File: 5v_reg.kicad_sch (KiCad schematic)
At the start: 19 parts, among them U3 IR3899A

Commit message: Added indicator LEDs and fixed some footprints
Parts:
- C16, C17, C18, C19, C26, C27, C28, Cboot, Cin, Co, Cvcc, Cvin: footprint Capacitor_SMD:C_0805_2012Metric_Pad1.18x1.45mm_HandSolder -> Capacitor_SMD:C_0805_2012Metric
- Cff: footprint Capacitor_SMD:C_0603_1608Metric_Pad1.08x0.95mm_HandSolder -> Capacitor_SMD:C_0603_1608Metric
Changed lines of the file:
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@@
       (effects (font (size 1.27 1.27)) (justify left))
     )
-    (property "Footprint" "Capacitor_SMD:C_0805_2012Metric_Pad1.18x1.45mm_HandSolder" (at 159.7152 91.44 0)
+    (property "Footprint" "Capacitor_SMD:C_0805_2012Metric" (at 159.7152 91.44 0)
       (effects (font (size 1.27 1.27)) hide)
     )
@@
       (effects (font (size 1.27 1.27)) (justify left))
     )
-    (property "Footprint" "Capacitor_SMD:C_0805_2012Metric_Pad1.18x1.45mm_HandSolder" (at 88.5952 69.85 0)
+    (property "Footprint" "Capacitor_SMD:C_0805_2012Metric" (at 88.5952 69.85 0)
       (effects (font (size 1.27 1.27)) hide)
     )
@@
       (effects (font (size 1.27 1.27)) (justify left))
     )
-    (property "Footprint" "Capacitor_SMD:C_0805_2012Metric_Pad1.18x1.45mm_HandSolder" (at 106.3752 69.85 0)
+    (property "Footprint" "Capacitor_SMD:C_0805_2012Metric" (at 106.3752 69.85 0)
       (effects (font (size 1.27 1.27)) hide)
     )
@@
       (effects (font (size 1.27 1.27)) (justify left))
     )
-    (property "Footprint" "Capacitor_SMD:C_0603_1608Metric_Pad1.08x0.95mm_HandSolder" (at 197.8152 102.87 0)
+    (property "Footprint" "Capacitor_SMD:C_0603_1608Metric" (at 197.8152 102.87 0)
       (effects (font (size 1.27 1.27)) hide)
     )
@@
       (effects (font (size 1.27 1.27)) (justify left))
     )
-    (property "Footprint" "Capacitor_SMD:C_0805_2012Metric_Pad1.18x1.45mm_HandSolder" (at 160.9852 67.31 0)
+    (property "Footprint" "Capacitor_SMD:C_0805_2012Metric" (at 160.9852 67.31 0)
       (effects (font (size 1.27 1.27)) hide)
     )
@@
       (effects (font (size 1.27 1.27)) (justify left))
     )
-    (property "Footprint" "Capacitor_SMD:C_0805_2012Metric_Pad1.18x1.45mm_HandSolder" (at 219.4052 100.33 0)
+    (property "Footprint" "Capacitor_SMD:C_0805_2012Metric" (at 219.4052 100.33 0)
       (effects (font (size 1.27 1.27)) hide)
     )
@@
       (effects (font (size 1.27 1.27)) (justify left))
     )
-    (property "Footprint" "Capacitor_SMD:C_0805_2012Metric_Pad1.18x1.45mm_HandSolder" (at 96.2152 69.85 0)
+    (property "Footprint" "Capacitor_SMD:C_0805_2012Metric" (at 96.2152 69.85 0)
       (effects (font (size 1.27 1.27)) hide)
     )
@@
       (effects (font (size 1.27 1.27)) (justify left))
     )
-    (property "Footprint" "Capacitor_SMD:C_0805_2012Metric_Pad1.18x1.45mm_HandSolder" (at 119.0752 69.85 0)
+    (property "Footprint" "Capacitor_SMD:C_0805_2012Metric" (at 119.0752 69.85 0)
       (effects (font (size 1.27 1.27)) hide)
     )
@@
       (effects (font (size 1.27 1.27)) (justify left))
     )
-    (property "Footprint" "Capacitor_SMD:C_0805_2012Metric_Pad1.18x1.45mm_HandSolder" (at 234.6452 100.33 0)
+    (property "Footprint" "Capacitor_SMD:C_0805_2012Metric" (at 234.6452 100.33 0)
       (effects (font (size 1.27 1.27)) hide)
     )
@@
       (effects (font (size 1.27 1.27)) (justify left))
     )
-    (property "Footprint" "Capacitor_SMD:C_0805_2012Metric_Pad1.18x1.45mm_HandSolder" (at 246.0752 100.33 0)
+    (property "Footprint" "Capacitor_SMD:C_0805_2012Metric" (at 246.0752 100.33 0)
       (effects (font (size 1.27 1.27)) hide)
     )
@@
       (effects (font (size 1.27 1.27)) (justify left))
     )
-    (property "Footprint" "Capacitor_SMD:C_0805_2012Metric_Pad1.18x1.45mm_HandSolder" (at 178.7652 99.06 0)
+    (property "Footprint" "Capacitor_SMD:C_0805_2012Metric" (at 178.7652 99.06 0)
       (effects (font (size 1.27 1.27)) hide)
     )
@@
       (effects (font (size 1.27 1.27)) (justify left))
     )
-    (property "Footprint" "Capacitor_SMD:C_0805_2012Metric_Pad1.18x1.45mm_HandSolder" (at 110.1852 85.09 0)
+    (property "Footprint" "Capacitor_SMD:C_0805_2012Metric" (at 110.1852 85.09 0)
       (effects (font (size 1.27 1.27)) hide)
     )
@@
       (effects (font (size 1.27 1.27)) (justify left))
     )
-    (property "Footprint" "Capacitor_SMD:C_0805_2012Metric_Pad1.18x1.45mm_HandSolder" (at 80.9752 69.85 0)
-      (effects (font (size 1.27 1.27)) hide)
-    )
+    (property "Footprint" "Capacitor_SMD:C_0805_2012Metric" (at 80.9752 69.85 0)
+      (effects (font (size 1.27 1.27)) hide)
+    )

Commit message: fixed some more footprints for resistors. 0201 -> 0603
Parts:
- R1, RFB1, RFB2, Rpg: footprint Resistor_SMD:R_0201_0603Metric -> Resistor_SMD:R_0603_1608Metric
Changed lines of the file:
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@@
       (effects (font (size 1.27 1.27)))
     )
-    (property "Footprint" "Resistor_SMD:R_0201_0603Metric" (at 152.654 82.804 90)
+    (property "Footprint" "Resistor_SMD:R_0603_1608Metric" (at 152.654 82.804 90)
       (effects (font (size 1.27 1.27)) hide)
     )
@@
       (effects (font (size 1.27 1.27)) (justify left))
     )
-    (property "Footprint" "Resistor_SMD:R_0201_0603Metric" (at 205.486 99.314 90)
+    (property "Footprint" "Resistor_SMD:R_0603_1608Metric" (at 205.486 99.314 90)
       (effects (font (size 1.27 1.27)) hide)
     )
@@
       (effects (font (size 1.27 1.27)) (justify left))
     )
-    (property "Footprint" "Resistor_SMD:R_0201_0603Metric" (at 205.486 109.474 90)
+    (property "Footprint" "Resistor_SMD:R_0603_1608Metric" (at 205.486 109.474 90)
       (effects (font (size 1.27 1.27)) hide)
     )
@@
       (effects (font (size 1.27 1.27)) (justify left))
     )
-    (property "Footprint" "Resistor_SMD:R_0201_0603Metric" (at 103.886 81.534 90)
-      (effects (font (size 1.27 1.27)) hide)
-    )
+    (property "Footprint" "Resistor_SMD:R_0603_1608Metric" (at 103.886 81.534 90)
+      (effects (font (size 1.27 1.27)) hide)
+    )

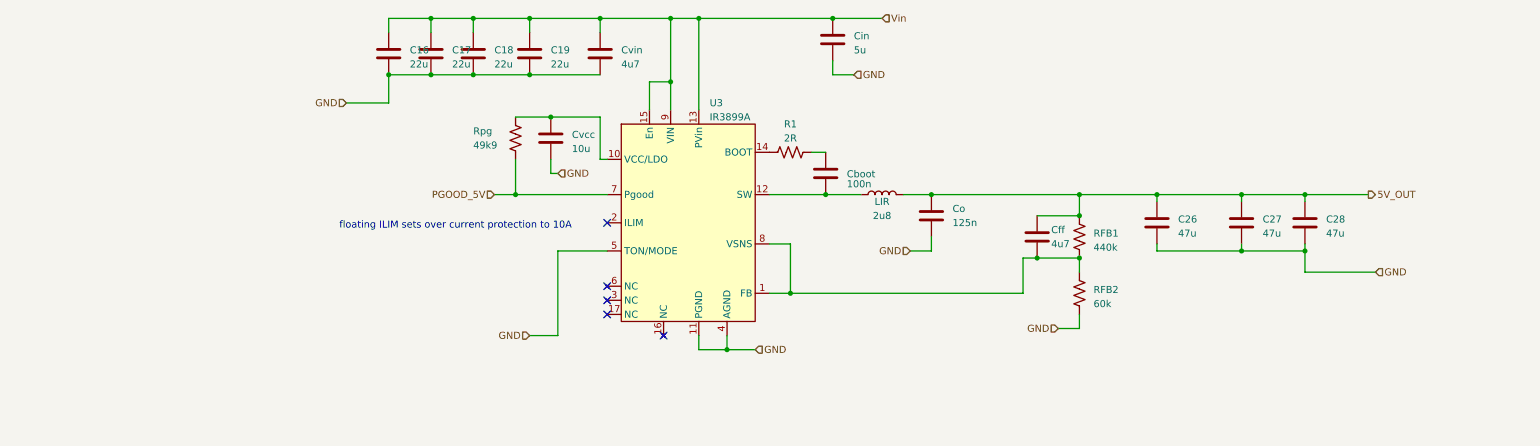
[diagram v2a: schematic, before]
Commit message: Changed 5V regulator and 12V regulator to the SiC461. Both support 10A and 5V and 12V respectively
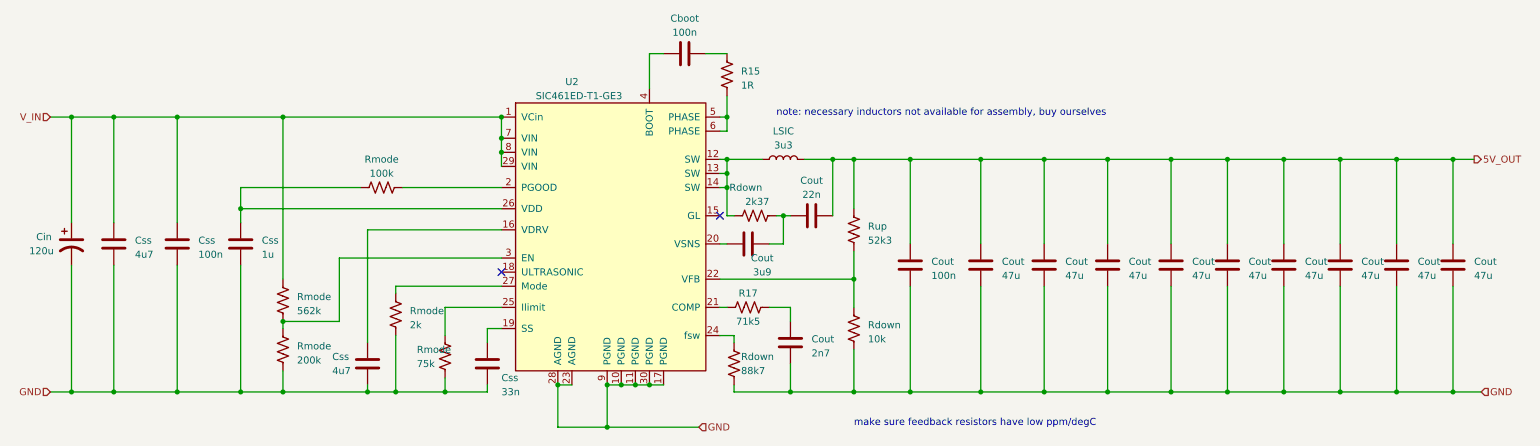
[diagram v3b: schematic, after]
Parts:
- removed C16, C17, C18, C19: 22u, Capacitor_SMD:C_0805_2012Metric, symbol Device:C
- removed C26, C27, C28: 47u, Capacitor_SMD:C_0805_2012Metric, symbol Device:C
- removed Cff: 4u7, Capacitor_SMD:C_0603_1608Metric, symbol Device:C
- removed Cin: 5u, Capacitor_SMD:C_0805_2012Metric, symbol Device:C
- removed Co: 125n, Capacitor_SMD:C_0805_2012Metric, symbol Device:C
- removed Cvcc: 10u, Capacitor_SMD:C_0805_2012Metric, symbol Device:C
- removed Cvin: 4u7, Capacitor_SMD:C_0805_2012Metric, symbol Device:C
- removed LIR: 2u8, crush-power-footprints:IND_1365-WE-HCI_WRE-L, symbol Device:L
- removed R1: 2R, Resistor_SMD:R_0603_1608Metric, symbol Device:R_US
- removed RFB1: 440k, Resistor_SMD:R_0603_1608Metric, symbol Device:R_US
- removed RFB2: 60k, Resistor_SMD:R_0603_1608Metric, symbol Device:R_US
- removed Rpg: 49k9, Resistor_SMD:R_0603_1608Metric, symbol Device:R_US
- removed U3: IR3899A, crush-power-footprints:IR3899AMTRPBFAUMA1, symbol crush-power-lib:IR3899A
- added Cin: 120u, Capacitor_Tantalum_SMD:CP_EIA-7343-15_Kemet-W, symbol Device:C_Polarized_US
- added Cout (x9): 47u, Capacitor_SMD:C_1210_3225Metric, symbol Device:C
- added Cout: 22n, Capacitor_SMD:C_0402_1005Metric, symbol Device:C
- added Cout: 3u9, Capacitor_SMD:C_0402_1005Metric, symbol Device:C
- added Cout, Css: 100n, Capacitor_SMD:C_0603_1608Metric, symbol Device:C
- added Cout: 2n7, Capacitor_SMD:C_0603_1608Metric, symbol Device:C
- added Css: 4u7, Capacitor_SMD:C_0603_1608Metric, symbol Device:C
- added Css: 33n, Capacitor_SMD:C_0603_1608Metric, symbol Device:C
- added Css: 4u7, Capacitor_SMD:C_0805_2012Metric, symbol Device:C
- added Css: 1u, Capacitor_SMD:C_0603_1608Metric, symbol Device:C
- added LSIC: 3u3, crush-power-footprints:IND_IHLP-6767GZ_VIS-M, symbol Device:L
- added R15: 1R, Resistor_SMD:R_0402_1005Metric, symbol Device:R_US
- added R17: 71k5, Resistor_SMD:R_0402_1005Metric, symbol Device:R_US
- added Rdown: 88k7, Resistor_SMD:R_0603_1608Metric, symbol Device:R_US
- added Rdown: 10k, Resistor_SMD:R_0603_1608Metric, symbol Device:R_US
- added Rdown: 2k37, Resistor_SMD:R_0402_1005Metric, symbol Device:R_US
- added Rmode: 75k, Resistor_SMD:R_0603_1608Metric, symbol Device:R_US
- added Rmode: 200k, Resistor_SMD:R_0603_1608Metric, symbol Device:R_US
- added Rmode: 562k, Resistor_SMD:R_0603_1608Metric, symbol Device:R_US
- added Rmode: 2k, Resistor_SMD:R_0603_1608Metric, symbol Device:R_US
- added Rmode: 100k, Resistor_SMD:R_0603_1608Metric, symbol Device:R_US
- added Rup: 52k3, Resistor_SMD:R_0603_1608Metric, symbol Device:R_US
- added U2: SIC461ED-T1-GE3, crush-power-footprints:CONV_SIC461ED-T1-GE3, symbol crush-power-lib:SIC461ED-T1-GE3
- Cboot: footprint Capacitor_SMD:C_0805_2012Metric -> Capacitor_SMD:C_0402_1005Metric
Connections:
- net 5V_OUT: now also Cout.1, Cout.1, Cout.1, Cout.1, Cout.1, Cout.1, Cout.1, Cout.1, Cout.1, Cout.1, Cout.2, LSIC.2, Rup.1
- net GND: now also Cin.2, Cout.2, Cout.2, Cout.2, Cout.2, Cout.2, Cout.2, Cout.2, Cout.2, Cout.2, Cout.2, Cout.2, Css.1, Css.1, Css.1, Css.1, Css.1, Rdown.2, Rdown.2, Rmode.1, Rmode.2, Rmode.2, U2.10 (PGND), U2.11 (PGND), U2.17 (PGND), U2.23 (AGND), U2.28 (AGND), U2.30 (PGND), U2.9 (PGND)
- net at Cboot.1: now also U2.4 (BOOT)
- net at Cboot.2: now also R15.2
- new net: R15.1, U2.5 (PHASE), U2.6 (PHASE)
- new net: Cout.1, Cout.2, Rdown.2
- new net: Css.2, U2.19 (SS)
- new net: Cout.1, U2.20 (VSNS)
- new net: R17.1, U2.21 (COMP)
- new net: Cout.1, R17.2
- new net: Css.2, U2.16 (VDRV)
- new net: Rdown.1, U2.24 (fsw)
- new net: Css.2, Rmode.1, U2.26 (VDD)
- new net: LSIC.1, Rdown.1, U2.12 (SW), U2.13 (SW), U2.14 (SW)
- new net: Rdown.1, Rup.2, U2.22 (VFB)
- new net: Rmode.2, U2.2 (PGOOD)
- new net: Rmode.1, U2.25 (Ilimit)
- new net: Rmode.1, U2.27 (Mode)
- new net: Rmode.1, Rmode.2, U2.3 (EN)
- new net V_IN: Cin.1, Css.2, Css.2, Rmode.2, U2.1 (VCin), U2.29 (VIN), U2.7 (VIN), U2.8 (VIN)
- no-connect marks 5 -> 2
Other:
- note added: "make sure feedback resistors have low ppm/degC"
- note added: "note: necessary inductors not available for assembly, buy ourselves"
- note removed: "floating ILIM sets over current protection to 10A"

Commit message: Added more to the layout of the 12V regulator as well as changed some capacitor footprints
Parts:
- Cin: footprint Capacitor_Tantalum_SMD:CP_EIA-7343-15_Kemet-W -> Capacitor_THT:CP_Radial_D8.0mm_P3.50mm
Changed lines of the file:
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@@
       (effects (font (size 1.27 1.27)) (justify left))
     )
-    (property "Footprint" "Capacitor_Tantalum_SMD:CP_EIA-7343-15_Kemet-W" (at 22.86 100.33 0)
+    (property "Footprint" "Capacitor_THT:CP_Radial_D8.0mm_P3.50mm" (at 22.86 100.33 0)
       (effects (font (size 1.27 1.27)) hide)
     )
@@
       (effects (font (size 1.27 1.27)) (justify bottom) hide)
     )
-    (property "Datasheet" "" (at 119.38 100.33 0)
-      (effects (font (size 1.27 1.27)) hide)
-    )
+    (property "Datasheet" "https://datasheet.lcsc.com/lcsc/2003271205_Vishay-Intertech-SIC461ED-T1-GE3_C499531.pdf" (at 119.38 100.33 0)
+      (effects (font (size 1.27 1.27)) hide)
+    )

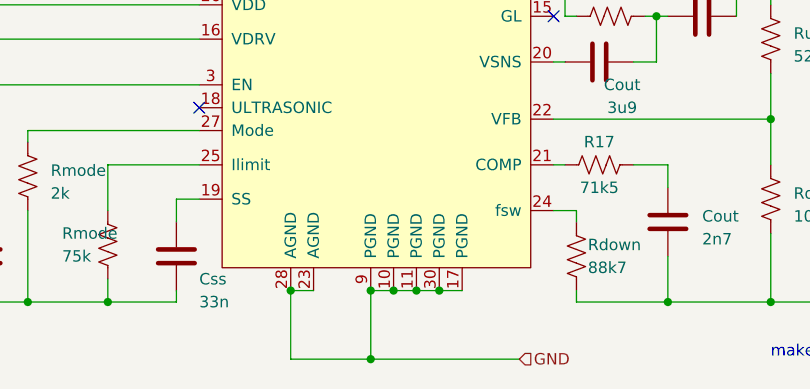
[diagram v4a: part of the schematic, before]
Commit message: Added thermal vias to the 12V regulator, fixed GND pad nets on 12V and 5V regulator
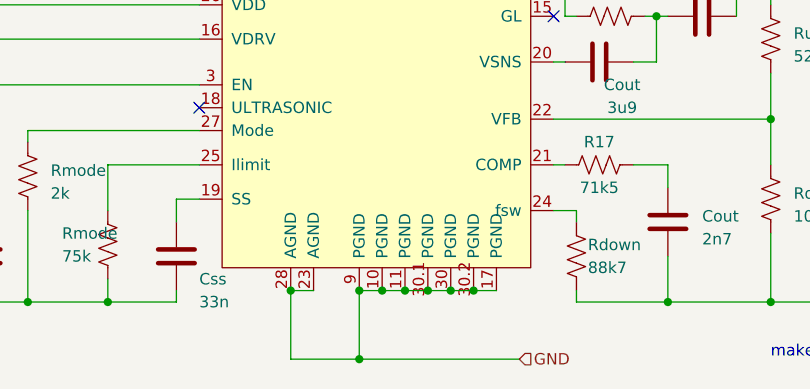
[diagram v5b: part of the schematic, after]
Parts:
- U2: footprint crush-power-footprints:CONV_SIC461ED-T1-GE3 -> CONV_SIC461ED-T1-GE3
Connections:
- net GND: now also U2.30.1 (PGND), U2.30.2 (PGND)
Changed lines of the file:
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@@
   (junction (at 53.34 93.98) (diameter 0) (color 0 0 0 0)
   )
-  (junction (at 119.38 125.73) (diameter 0) (color 0 0 0 0)
-  )
   (junction (at 251.46 127) (diameter 0) (color 0 0 0 0)
   )
@@
   (junction (at 30.48 127) (diameter 0) (color 0 0 0 0)
   )
+  (junction (at 125.73 125.73) (diameter 0) (color 0 0 0 0)
+  )
+  (junction (at 120.65 125.73) (diameter 0) (color 0 0 0 0)
+  )
   (junction (at 261.62 85.09) (diameter 0) (color 0 0 0 0)
   )
+  (junction (at 118.11 125.73) (diameter 0) (color 0 0 0 0)
+  )
   (junction (at 271.78 85.09) (diameter 0) (color 0 0 0 0)
   )
+  (junction (at 130.81 125.73) (diameter 0) (color 0 0 0 0)
+  )
   (junction (at 251.46 85.09) (diameter 0) (color 0 0 0 0)
   )
@@
   (junction (at 261.62 127) (diameter 0) (color 0 0 0 0)
   )
+  (junction (at 128.27 125.73) (diameter 0) (color 0 0 0 0)
+  )
   (junction (at 90.17 127) (diameter 0) (color 0 0 0 0)
   )
@@
   (junction (at 163.83 106.68) (diameter 0) (color 0 0 0 0)
   )
+  (junction (at 118.11 133.35) (diameter 0) (color 0 0 0 0)
+  )
   (junction (at 160.02 85.09) (diameter 0) (color 0 0 0 0)
   )
@@
   (junction (at 110.49 125.73) (diameter 0) (color 0 0 0 0)
   )
-  (junction (at 124.46 125.73) (diameter 0) (color 0 0 0 0)
-  )
   (junction (at 41.91 127) (diameter 0) (color 0 0 0 0)
   )
@@
   (junction (at 60.96 77.47) (diameter 0) (color 0 0 0 0)
   )
+  (junction (at 123.19 125.73) (diameter 0) (color 0 0 0 0)
+  )
   (junction (at 186.69 127) (diameter 0) (color 0 0 0 0)
   )
@@
   (junction (at 152.4 127) (diameter 0) (color 0 0 0 0)
   )
-  (junction (at 119.38 133.35) (diameter 0) (color 0 0 0 0)
-  )
   (junction (at 231.14 85.09) (diameter 0) (color 0 0 0 0)
   )
@@
   (junction (at 81.28 127) (diameter 0) (color 0 0 0 0)
   )
-  (junction (at 121.92 125.73) (diameter 0) (color 0 0 0 0)
-  )
   (junction (at 209.55 85.09) (diameter 0) (color 0 0 0 0)
   )
   (junction (at 198.12 85.09) (diameter 0) (color 0 0 0 0)
-  )
-  (junction (at 127 125.73) (diameter 0) (color 0 0 0 0)
   )
   (no_connect (at 139.7 95.25))
@@
     (stroke (width 0) (type default))
   )
-  (wire (pts (xy 119.38 133.35) (xy 135.89 133.35))
-    (stroke (width 0) (type default))
-  )
   (wire (pts (xy 140.97 80.01) (xy 139.7 80.01))
     (stroke (width 0) (type default))
@@
     (stroke (width 0) (type default))
   )
-  (wire (pts (xy 119.38 125.73) (xy 121.92 125.73))
-    (stroke (width 0) (type default))
-  )
   (wire (pts (xy 261.62 107.95) (xy 261.62 127))
     (stroke (width 0) (type default))
@@
     (stroke (width 0) (type default))
   )
-  (wire (pts (xy 119.38 125.73) (xy 119.38 133.35))
+  (wire (pts (xy 118.11 125.73) (xy 118.11 133.35))
+    (stroke (width 0) (type default))
+  )
+  (wire (pts (xy 128.27 125.73) (xy 130.81 125.73))
     (stroke (width 0) (type default))
   )
@@
     (stroke (width 0) (type default))
   )
+  (wire (pts (xy 118.11 133.35) (xy 135.89 133.35))
+    (stroke (width 0) (type default))
+  )
   (wire (pts (xy 271.78 127) (xy 276.86 127))
     (stroke (width 0) (type default))
@@
     (stroke (width 0) (type default))
   )
-  (wire (pts (xy 121.92 125.73) (xy 124.46 125.73))
-    (stroke (width 0) (type default))
-  )
   (wire (pts (xy 160.02 85.09) (xy 160.02 95.25))
     (stroke (width 0) (type default))
@@
     (stroke (width 0) (type default))
   )
-  (wire (pts (xy 124.46 125.73) (xy 127 125.73))
-    (stroke (width 0) (type default))
-  )
   (wire (pts (xy 261.62 85.09) (xy 261.62 100.33))
     (stroke (width 0) (type default))
@@
     (stroke (width 0) (type default))
   )
+  (wire (pts (xy 130.81 125.73) (xy 133.35 125.73))
+    (stroke (width 0) (type default))
+  )
   (wire (pts (xy 140.97 77.47) (xy 140.97 80.01))
     (stroke (width 0) (type default))
@@
     (stroke (width 0) (type default))
   )
-  (wire (pts (xy 127 125.73) (xy 129.54 125.73))
+  (wire (pts (xy 118.11 125.73) (xy 120.65 125.73))
     (stroke (width 0) (type default))
   )
@@
     (stroke (width 0) (type default))
   )
-  (wire (pts (xy 110.49 133.35) (xy 119.38 133.35))
+  (wire (pts (xy 110.49 133.35) (xy 118.11 133.35))
     (stroke (width 0) (type default))
   )
@@
     (stroke (width 0) (type default))
   )
+  (wire (pts (xy 125.73 125.73) (xy 128.27 125.73))
+    (stroke (width 0) (type default))
+  )
   (wire (pts (xy 173.99 127) (xy 186.69 127))
     (stroke (width 0) (type default))
@@
     (stroke (width 0) (type default))
   )
+  (wire (pts (xy 120.65 125.73) (xy 123.19 125.73))
+    (stroke (width 0) (type default))
+  )
   (wire (pts (xy 22.86 104.14) (xy 22.86 127))
     (stroke (width 0) (type default))
@@
   )
   (wire (pts (xy 129.54 66.04) (xy 127 66.04))
+    (stroke (width 0) (type default))
+  )
+  (wire (pts (xy 123.19 125.73) (xy 125.73 125.73))
     (stroke (width 0) (type default))
   )
@@
       (effects (font (size 1.27 1.27)))
     )
-    (property "Footprint" "crush-power-footprints:CONV_SIC461ED-T1-GE3" (at 119.38 100.33 0)
+    (property "Footprint" "CONV_SIC461ED-T1-GE3" (at 119.38 100.33 0)
       (effects (font (size 1.27 1.27)) (justify bottom) hide)
     )
@@
     (pin "3")
     (pin "30")
+    (pin "30.1")
+    (pin "30.2")
     (pin "4")
     (pin "5")

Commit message: fix batt_t planes
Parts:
- renumbered Cin to C25, Css to C26, Css to C27, Css to C28, Css to C29, Css to C30, Cboot to C31, Cout to C32, Cout to C33, Cout to C34, Cout to C35, Cout to C36, Cout to C37, Cout to C38, Cout to C39, Cout to C40, Cout to C41, Cout to C42, Cout to C43, Cout to C44, LSIC to L3, Rmode to R22, Rmode to R23, Rmode to R24, Rmode to R25, Rmode to R26, R15 to R27, Rdown to R28, R17 to R29, Rdown to R30, Rup to R31, Rdown to R32, U2 to U3
